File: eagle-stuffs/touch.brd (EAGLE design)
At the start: 152.1 x 25.4 mm, 6 parts, among them U1 AT42QT1010SOT23

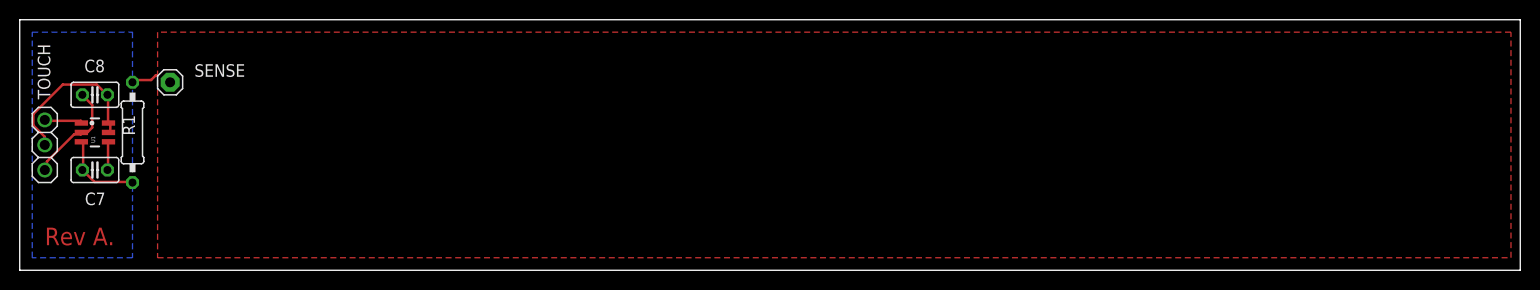
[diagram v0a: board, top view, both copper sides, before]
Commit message: Changed some drilling size
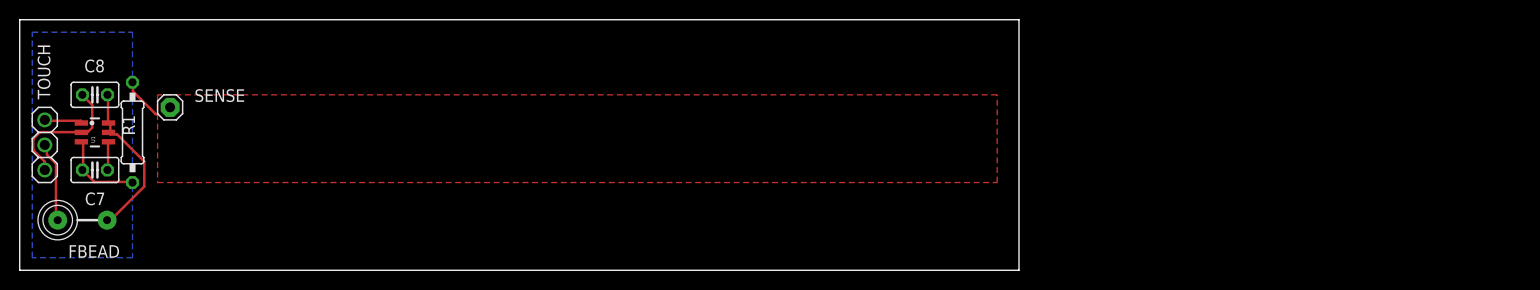
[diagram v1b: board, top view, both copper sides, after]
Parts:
- added FBEAD: FB, adafruit:FB
- moved SENSE 2.54 mm to (15.2, 16.5)
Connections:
- new net N$3: FBEAD.P$2, TOUCH.2
- net +5V: now also FBEAD.P$1; no longer TOUCH.2
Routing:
- net N$3: track 0.00 -> 8.22 mm
- net GND: track 10.8 -> 13.8 mm
- net N$2: track 2.92 -> 4.42 mm
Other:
- board size 152.1 x 25.4 mm -> 101.3 x 25.4 mm
- board text removed: "Rev A."
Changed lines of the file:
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@@
 <board>
 <plain>
-<wire x1="0" y1="0" x2="152.07" y2="0" width="0" layer="20"/>
-<wire x1="152.07" y1="0" x2="152.07" y2="25.39" width="0" layer="20"/>
-<wire x1="152.07" y1="25.39" x2="0" y2="25.39" width="0" layer="20"/>
+<wire x1="0" y1="0" x2="101.27" y2="0" width="0" layer="20"/>
+<wire x1="101.27" y1="0" x2="101.27" y2="25.39" width="0" layer="20"/>
+<wire x1="101.27" y1="25.39" x2="0" y2="25.39" width="0" layer="20"/>
 <wire x1="0" y1="25.39" x2="0" y2="0" width="0" layer="20"/>
-<text x="2.54" y="2.54" size="1.778" layer="1">Rev A.</text>
-<rectangle x1="2.54" y1="2.54" x2="11.43" y2="5.08" layer="39"/>
 </plain>
 <attributes>
@@
 <attribute name="VALUE" x="-0.635" y="16.51" size="1.27" layer="27" rot="R270"/>
 </element>
-<element name="SENSE" library="adafruit" package="1X01" value="" x="15.24" y="19.05" smashed="yes">
-<attribute name="NAME" x="17.7038" y="19.6088" size="1.27" layer="25" ratio="10"/>
-<attribute name="VALUE" x="13.97" y="15.875" size="1.27" layer="27"/>
-</element>
+<element name="SENSE" library="adafruit" package="1X01" value="" x="15.24" y="16.51" smashed="yes">
+<attribute name="NAME" x="17.7038" y="17.0688" size="1.27" layer="25" ratio="10"/>
+<attribute name="VALUE" x="13.97" y="13.335" size="1.27" layer="27"/>
+</element>
+<element name="FBEAD" library="adafruit" package="FB" value="FB" x="6.35" y="5.08" rot="R180"/>
 </elements>
 <signals>
@@
 <contactref element="C8" pad="2"/>
 <contactref element="TOUCH" pad="3"/>
+<polygon width="0.4064" layer="16">
+<vertex x="1.27" y="24.13"/>
+<vertex x="11.43" y="24.13"/>
+<vertex x="11.43" y="1.27"/>
+<vertex x="1.27" y="1.27"/>
+</polygon>
 <wire x1="6.885" y1="13.9995" x2="6.426" y2="13.9995" width="0.254" layer="1"/>
 <wire x1="7.344" y1="14.4585" x2="6.885" y2="13.9995" width="0.254" layer="1"/>
@@
 <wire x1="6.426" y1="13.9995" x2="6.2449" y2="13.97" width="0.254" layer="1"/>
 <wire x1="6.426" y1="17.6715" x2="6.35" y2="17.78" width="0.254" layer="1"/>
-<wire x1="2.754" y1="11.016" x2="2.754" y2="10.3275" width="0.254" layer="1"/>
-<wire x1="5.508" y1="13.77" x2="2.754" y2="11.016" width="0.254" layer="1"/>
-<wire x1="6.1965" y1="13.77" x2="5.508" y2="13.77" width="0.254" layer="1"/>
-<wire x1="2.754" y1="10.3275" x2="2.54" y2="10.16" width="0.254" layer="1"/>
-<wire x1="6.1965" y1="13.77" x2="6.2449" y2="13.97" width="0.254" layer="1"/>
-<polygon width="0.4064" layer="16">
-<vertex x="1.27" y="24.13"/>
-<vertex x="11.43" y="24.13"/>
-<vertex x="11.43" y="1.27"/>
-<vertex x="1.27" y="1.27"/>
-</polygon>
+<wire x1="2.5245" y1="11.016" x2="2.5245" y2="10.3275" width="0.254" layer="1"/>
+<wire x1="1.377" y1="12.1635" x2="2.5245" y2="11.016" width="0.254" layer="1"/>
+<wire x1="1.377" y1="13.311" x2="1.377" y2="12.1635" width="0.254" layer="1"/>
+<wire x1="2.0655" y1="13.9995" x2="1.377" y2="13.311" width="0.254" layer="1"/>
+<wire x1="6.1965" y1="13.9995" x2="2.0655" y2="13.9995" width="0.254" layer="1"/>
+<wire x1="2.5245" y1="10.3275" x2="2.54" y2="10.16" width="0.254" layer="1"/>
+<wire x1="6.1965" y1="13.9995" x2="6.2449" y2="13.97" width="0.254" layer="1"/>
 </signal>
 <signal name="+5V">
@@
 <contactref element="U1" pad="6"/>
 <contactref element="C8" pad="1"/>
-<contactref element="TOUCH" pad="2"/>
+<contactref element="FBEAD" pad="P$1"/>
 <wire x1="9.18" y1="14.9175" x2="9.18" y2="13.9995" width="0.254" layer="1"/>
 <wire x1="9.18" y1="13.9995" x2="8.9951" y2="13.97" width="0.254" layer="1"/>
@@
 <wire x1="8.9505" y1="15.147" x2="8.9951" y2="14.92" width="0.254" layer="1"/>
 <wire x1="8.9505" y1="17.6715" x2="8.89" y2="17.78" width="0.254" layer="1"/>
-<wire x1="2.5245" y1="13.5405" x2="2.5245" y2="12.852" width="0.254" layer="1"/>
-<wire x1="1.377" y1="14.688" x2="2.5245" y2="13.5405" width="0.254" layer="1"/>
-<wire x1="1.377" y1="15.8355" x2="1.377" y2="14.688" width="0.254" layer="1"/>
-<wire x1="4.3605" y1="18.819" x2="1.377" y2="15.8355" width="0.254" layer="1"/>
-<wire x1="7.803" y1="18.819" x2="4.3605" y2="18.819" width="0.254" layer="1"/>
-<wire x1="8.721" y1="17.901" x2="7.803" y2="18.819" width="0.254" layer="1"/>
-<wire x1="2.5245" y1="12.852" x2="2.54" y2="12.7" width="0.254" layer="1"/>
-<wire x1="8.721" y1="17.901" x2="8.89" y2="17.78" width="0.254" layer="1"/>
+<wire x1="9.8685" y1="13.77" x2="9.18" y2="13.77" width="0.254" layer="1"/>
+<wire x1="12.6225" y1="11.016" x2="9.8685" y2="13.77" width="0.254" layer="1"/>
+<wire x1="12.6225" y1="8.4915" x2="12.6225" y2="11.016" width="0.254" layer="1"/>
+<wire x1="9.4095" y1="5.2785" x2="12.6225" y2="8.4915" width="0.254" layer="1"/>
+<wire x1="8.9505" y1="5.2785" x2="9.4095" y2="5.2785" width="0.254" layer="1"/>
+<wire x1="9.18" y1="13.77" x2="8.9951" y2="13.97" width="0.254" layer="1"/>
+<wire x1="8.9505" y1="5.2785" x2="8.85" y2="5.08" width="0.254" layer="1"/>
 </signal>
 <signal name="N$16">
@@
 <contactref element="R1" pad="1"/>
 <polygon width="0.4064" layer="1">
-<vertex x="13.97" y="24.13"/>
-<vertex x="13.97" y="1.27"/>
-<vertex x="151.13" y="1.27"/>
-<vertex x="151.13" y="24.13"/>
+<vertex x="13.97" y="17.78"/>
+<vertex x="13.97" y="8.89"/>
+<vertex x="99.06" y="8.89"/>
+<vertex x="99.06" y="17.78"/>
 </polygon>
-<wire x1="13.311" y1="19.278" x2="11.475" y2="19.278" width="0.254" layer="1"/>
-<wire x1="13.77" y1="19.737" x2="13.311" y2="19.278" width="0.254" layer="1"/>
-<wire x1="11.475" y1="19.278" x2="11.43" y2="19.05" width="0.254" layer="1"/>
-<wire x1="13.77" y1="19.737" x2="13.97" y2="19.791571875" width="0.254" layer="1"/>
+<wire x1="11.475" y1="18.1305" x2="11.475" y2="19.0485" width="0.254" layer="1"/>
+<wire x1="13.77" y1="15.8355" x2="11.475" y2="18.1305" width="0.254" layer="1"/>
+<wire x1="11.475" y1="19.0485" x2="11.43" y2="19.05" width="0.254" layer="1"/>
+<wire x1="13.77" y1="15.8355" x2="13.97" y2="15.768425" width="0.254" layer="1"/>
+</signal>
+<signal name="N$3">
+<contactref element="TOUCH" pad="2"/>
+<contactref element="FBEAD" pad="P$2"/>
+<wire x1="2.754" y1="11.7045" x2="2.754" y2="12.6225" width="0.254" layer="1"/>
+<wire x1="3.672" y1="10.7865" x2="2.754" y2="11.7045" width="0.254" layer="1"/>
+<wire x1="3.672" y1="5.2785" x2="3.672" y2="10.7865" width="0.254" layer="1"/>
+<wire x1="2.754" y1="12.6225" x2="2.54" y2="12.7" width="0.254" layer="1"/>
+<wire x1="3.672" y1="5.2785" x2="3.85" y2="5.08" width="0.254" layer="1"/>
 </signal>
 </signals>

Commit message: Added some info
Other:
- board text added: "Rev. A"
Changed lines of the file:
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@@
 <wire x1="101.27" y1="25.39" x2="0" y2="25.39" width="0" layer="20"/>
 <wire x1="0" y1="25.39" x2="0" y2="0" width="0" layer="20"/>
+<text x="12.7" y="1.27" size="1.778" layer="25">Rev. A</text>
 </plain>
 <attributes>
@@
 </element>
 <element name="SENSE" library="adafruit" package="1X01" value="" x="15.24" y="16.51" smashed="yes">
-<attribute name="NAME" x="17.7038" y="17.0688" size="1.27" layer="25" ratio="10"/>
+<attribute name="NAME" x="16.4338" y="18.3388" size="1.27" layer="25" ratio="10"/>
 <attribute name="VALUE" x="13.97" y="13.335" size="1.27" layer="27"/>
 </element>
